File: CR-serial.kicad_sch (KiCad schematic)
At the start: 34 parts, among them J1 USB_B, J2 GPIO, J3 UART0, J4 UART1, J5 UART2, J6 UART3_HV, J7 RS232_0, J8 RS232_1, U1 CP2108-xxx-xM, U2 MAX232

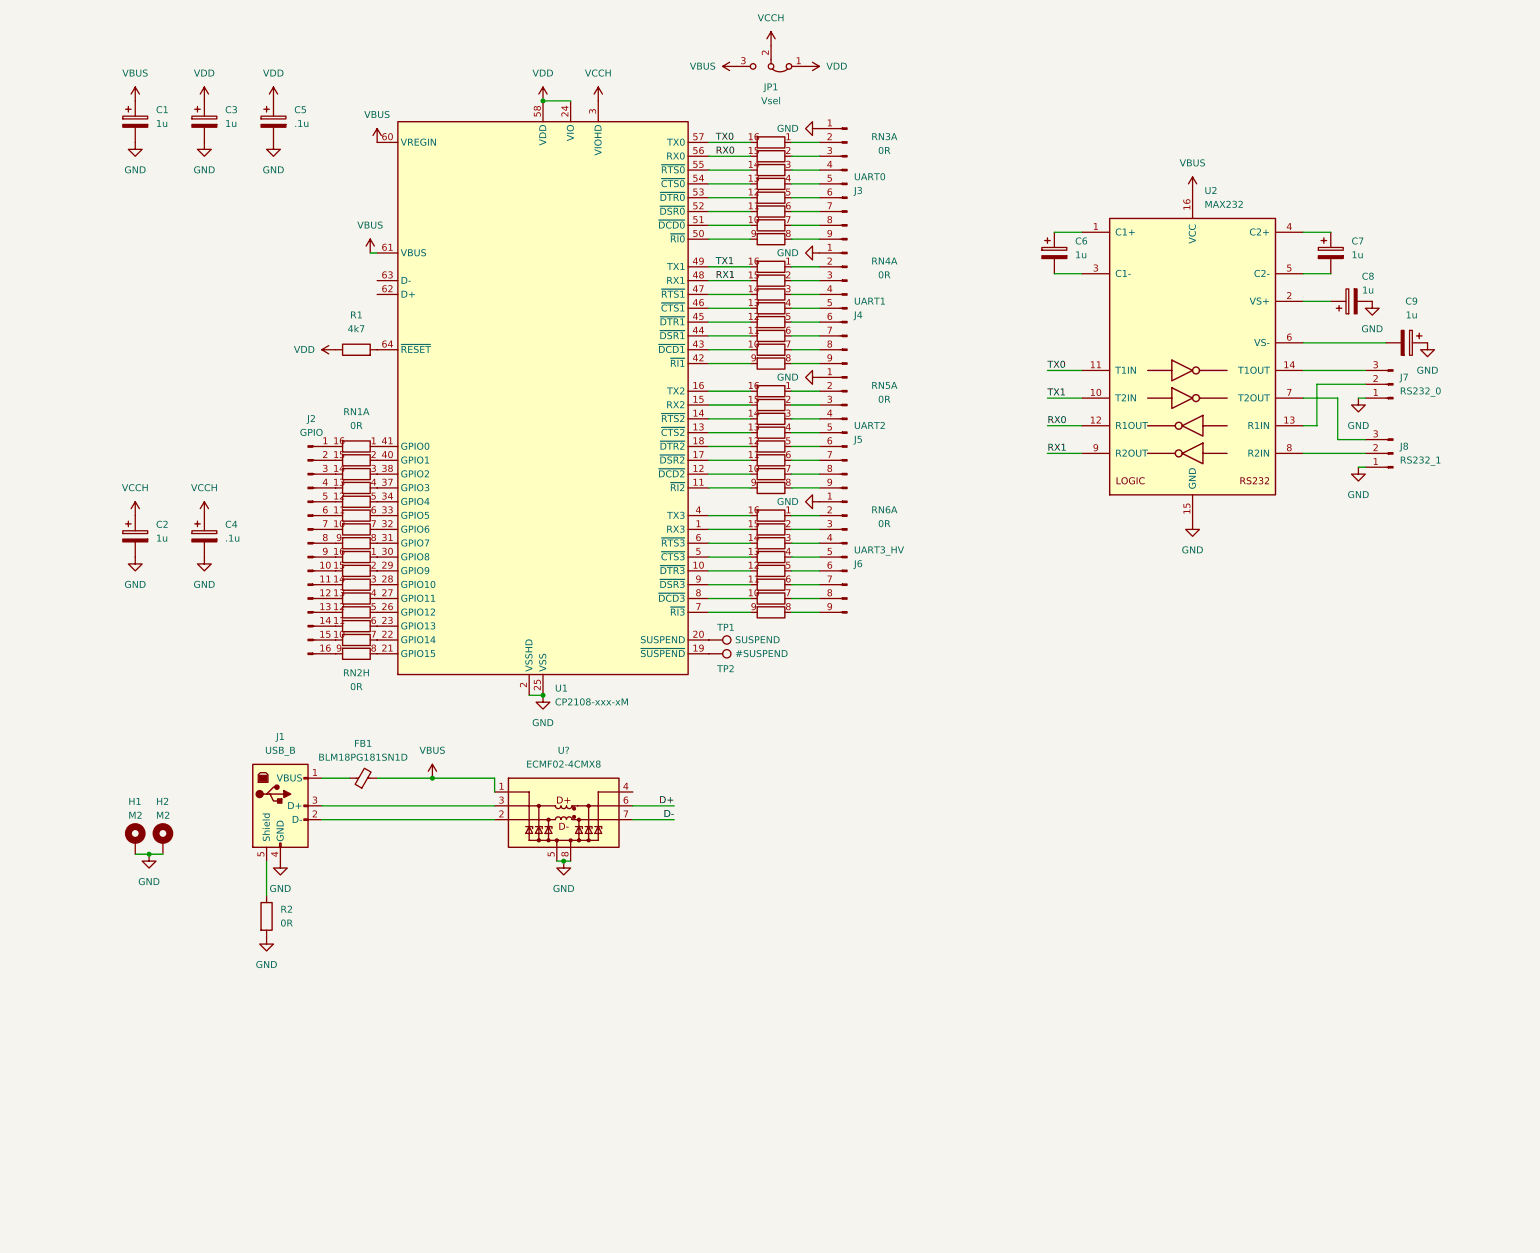
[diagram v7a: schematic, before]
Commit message: UARTs: Rework ESD protection, use individual Rs, add TVS
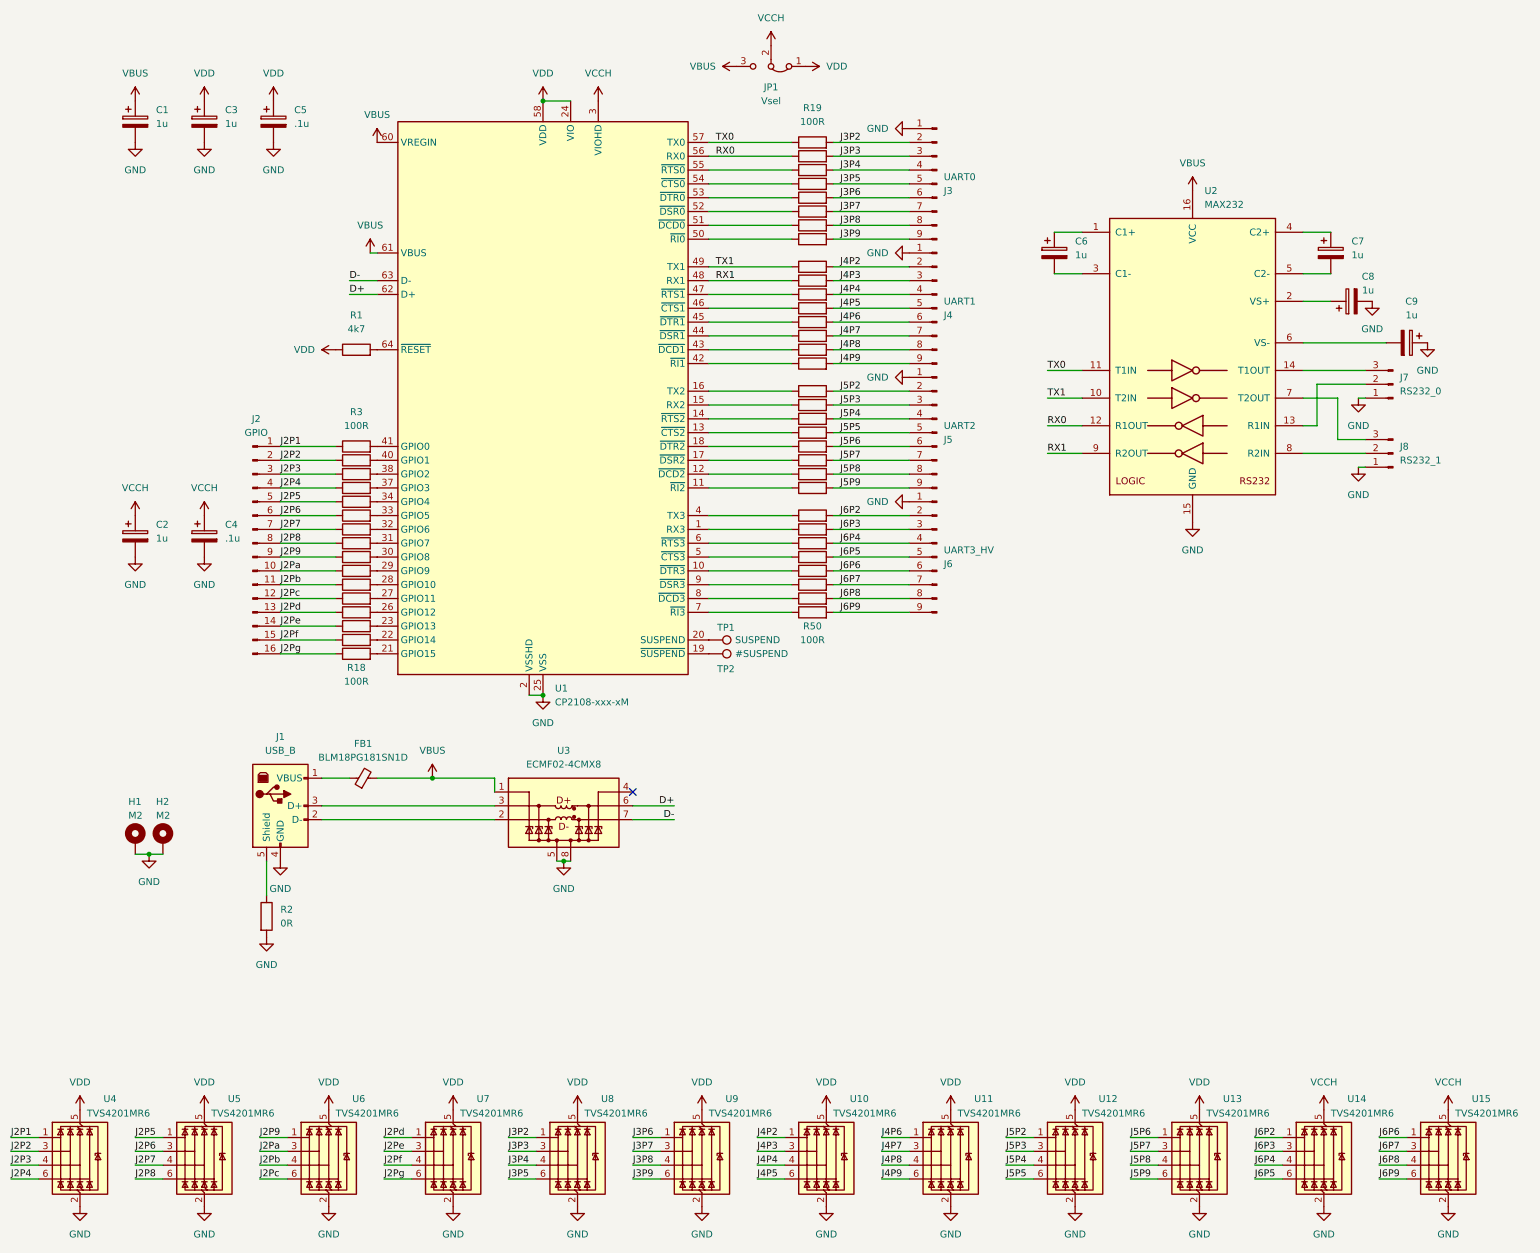
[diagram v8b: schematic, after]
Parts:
- removed RN1, RN2, RN3, RN4, RN5, RN6: 0R, Resistor_SMD:R_Array_Convex_8x0602, symbol Device:R_Pack08_Split
- added R10, R11, R12, R13, R14, R15, R16, R17, R18, R19, R20, R21, R22, R23, R24, R25, R26, R27, R28, R29, R3, R30, R31, R32, R33, R34, R35, R36, R37, R38, R39, R4, R40, R41, R42, R43, R44, R45, R46, R47, R48, R49, R5, R50, R6, R7, R8, R9: 100R, Resistor_SMD:R_0603_1608Metric, symbol Device:R
- added U10, U11, U12, U13, U14, U15, U4, U5, U6, U7, U8, U9: TVS4201MR6, Package_SO:TSOP-6_1.65x3.05mm_P0.95mm, symbol QCP_parts:TVS4201MR6
- gave numbers to parts that had none: 1
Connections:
- net D+: now also U1.62 (D+)
- net D-: now also U1.63 (D-)
- net GND: now also U10.2 (GND), U11.2 (GND), U12.2 (GND), U13.2 (GND), U14.2 (GND), U15.2 (GND), U4.2 (GND), U5.2 (GND), U6.2 (GND), U7.2 (GND), U8.2 (GND), U9.2 (GND)
- net RX0: now also R20.1
- net RX1: now also R28.1
- net TX0: now also R19.1
- net TX1: now also R27.1
- net VCCH: now also U14.5 (VBUS), U15.5 (VBUS)
- net VDD: now also U10.5 (VBUS), U11.5 (VBUS), U12.5 (VBUS), U13.5 (VBUS), U4.5 (VBUS), U5.5 (VBUS), U6.5 (VBUS), U7.5 (VBUS), U8.5 (VBUS), U9.5 (VBUS)
- net at U1.1 (RX3): now also R44.1
- net at U1.10 (~{DTR3}): now also R47.1
- net at U1.11 (~{RI2}): now also R42.1
- net at U1.12 (~{DCD2}): now also R41.1
- net at U1.13 (~{CTS2}): now also R38.1
- net at U1.14 (~{RTS2}): now also R37.1
- net at U1.15 (RX2): now also R36.1
- net at U1.16 (TX2): now also R35.1
- net at U1.17 (~{DSR2}): now also R40.1
- net at U1.18 (~{DTR2}): now also R39.1
- net at U1.21 (GPIO15): now also R18.2
- net at U1.22 (GPIO14): now also R17.2
- net at U1.23 (GPIO13): now also R16.2
- net at U1.26 (GPIO12): now also R15.2
- net at U1.27 (GPIO11): now also R14.2
- net at U1.28 (GPIO10): now also R13.2
- net at U1.29 (GPIO9): now also R12.2
- net at U1.30 (GPIO8): now also R11.2
- net at U1.31 (GPIO7): now also R10.2
- net at U1.32 (GPIO6): now also R9.2
- net at U1.33 (GPIO5): now also R8.2
- net at U1.34 (GPIO4): now also R7.2
- net at U1.37 (GPIO3): now also R6.2
- net at U1.38 (GPIO2): now also R5.2
- net at U1.4 (TX3): now also R43.1
- net at U1.40 (GPIO1): now also R4.2
- net at U1.41 (GPIO0): now also R3.2
- net at U1.42 (~{RI1}): now also R34.1
- net at U1.43 (~{DCD1}): now also R33.1
- net at U1.44 (~{DSR1}): now also R32.1
- net at U1.45 (~{DTR1}): now also R31.1
- net at U1.46 (~{CTS1}): now also R30.1
- net at U1.47 (~{RTS1}): now also R29.1
- net at U1.5 (~{CTS3}): now also R46.1
- net at U1.50 (~{RI0}): now also R26.1
- net at U1.51 (~{DCD0}): now also R25.1
- net at U1.52 (~{DSR0}): now also R24.1
- net at U1.53 (~{DTR0}): now also R23.1
- net at U1.54 (~{CTS0}): now also R22.1
- net at U1.55 (~{RTS0}): now also R21.1
- net at U1.6 (~{RTS3}): now also R45.1
- net at U1.7 (~{RI3}): now also R50.1
- net at U1.8 (~{DCD3}): now also R49.1
- net at U1.9 (~{DSR3}): now also R48.1
- net J4P5: now reaches J4.5 (Pin_5)
- net J4P5: now also R30.2, U10.6 (I/O4)
- net J5P2: now reaches J5.2 (Pin_2)
- net J5P2: now also R35.2, U12.1 (I/O1)
- net J3P8: now reaches J3.8 (Pin_8)
- net J3P8: now also R25.2, U9.4 (I/O3)
- net J2P1: now reaches J2.1 (Pin_1)
- net J2P1: now also R3.1, U4.1 (I/O1)
- net J2Pd: now reaches J2.13 (Pin_13)
- net J2Pd: now also R15.1, U7.1 (I/O1)
- net J6P9: now reaches J6.9 (Pin_9)
- net J6P9: now also R50.2, U15.6 (I/O4)
- net J4P6: now reaches J4.6 (Pin_6)
- net J4P6: now also R31.2, U11.1 (I/O1)
- net J5P3: now reaches J5.3 (Pin_3)
- net J5P3: now also R36.2, U12.3 (I/O2)
- net J5P4: now reaches J5.4 (Pin_4)
- net J5P4: now also R37.2, U12.4 (I/O3)
- net J5P5: now reaches J5.5 (Pin_5)
- net J5P5: now also R38.2, U12.6 (I/O4)
- net J5P6: now reaches J5.6 (Pin_6)
- net J5P6: now also R39.2, U13.1 (I/O1)
- net J5P7: now reaches J5.7 (Pin_7)
- net J5P7: now also R40.2, U13.3 (I/O2)
- net J5P8: now reaches J5.8 (Pin_8)
- net J5P8: now also R41.2, U13.4 (I/O3)
- net J5P9: now reaches J5.9 (Pin_9)
- net J5P9: now also R42.2, U13.6 (I/O4)
- net J2Pa: now reaches J2.10 (Pin_10)
- net J2Pa: now also R12.1, U6.3 (I/O2)
- net J2P4: now reaches J2.4 (Pin_4)
- net J2P4: now also R6.1, U4.6 (I/O4)
- net J6P7: now reaches J6.7 (Pin_7)
- net J6P7: now also R48.2, U15.3 (I/O2)
- net J6P2: now reaches J6.2 (Pin_2)
- net J6P2: now also R43.2, U14.1 (I/O1)
- net J6P3: now reaches J6.3 (Pin_3)
- net J6P3: now also R44.2, U14.3 (I/O2)
- net J6P4: now reaches J6.4 (Pin_4)
- net J6P4: now also R45.2, U14.4 (I/O3)
- net J6P5: now reaches J6.5 (Pin_5)
- net J6P5: now also R46.2, U14.6 (I/O4)
- net J6P6: now reaches J6.6 (Pin_6)
- net J6P6: now also R47.2, U15.1 (I/O1)
- net J6P8: now reaches J6.8 (Pin_8)
- net J6P8: now also R49.2, U15.4 (I/O3)
- net J2Pg: now reaches J2.16 (Pin_16)
- net J2Pg: now also R18.1, U7.6 (I/O4)
- net J3P3: now reaches J3.3 (Pin_3)
- net J3P3: now also R20.2, U8.3 (I/O2)
- net J2Pc: now reaches J2.12 (Pin_12)
- net J2Pc: now also R14.1, U6.6 (I/O4)
- net J3P7: now reaches J3.7 (Pin_7)
- net J3P7: now also R24.2, U9.3 (I/O2)
- net J3P2: now reaches J3.2 (Pin_2)
- net J3P2: now also R19.2, U8.1 (I/O1)
- net J3P4: now reaches J3.4 (Pin_4)
- net J3P4: now also R21.2, U8.4 (I/O3)
- net J3P5: now reaches J3.5 (Pin_5)
- net J3P5: now also R22.2, U8.6 (I/O4)
- net J3P6: now reaches J3.6 (Pin_6)
- net J3P6: now also R23.2, U9.1 (I/O1)
- net J3P9: now reaches J3.9 (Pin_9)
- net J3P9: now also R26.2, U9.6 (I/O4)
- net J4P8: now reaches J4.8 (Pin_8)
- net J4P8: now also R33.2, U11.4 (I/O3)
- net J4P2: now reaches J4.2 (Pin_2)
- net J4P2: now also R27.2, U10.1 (I/O1)
- net J4P3: now reaches J4.3 (Pin_3)
- net J4P3: now also R28.2, U10.3 (I/O2)
- net J4P4: now reaches J4.4 (Pin_4)
- net J4P4: now also R29.2, U10.4 (I/O3)
- net J4P7: now reaches J4.7 (Pin_7)
- net J4P7: now also R32.2, U11.3 (I/O2)
- net J4P9: now reaches J4.9 (Pin_9)
- net J4P9: now also R34.2, U11.6 (I/O4)
- net J2Pe: now reaches J2.14 (Pin_14)
- net J2Pe: now also R16.1, U7.3 (I/O2)
- net J2P9: now reaches J2.9 (Pin_9)
- net J2P9: now also R11.1, U6.1 (I/O1)
- net J2P3: now reaches J2.3 (Pin_3)
- net J2P3: now also R5.1, U4.4 (I/O3)
- net J2P6: now reaches J2.6 (Pin_6)
- net J2P6: now also R8.1, U5.3 (I/O2)
- net J2Pf: now reaches J2.15 (Pin_15)
- net J2Pf: now also R17.1, U7.4 (I/O3)
- net J2P5: now reaches J2.5 (Pin_5)
- net J2P5: now also R7.1, U5.1 (I/O1)
- net J2P8: now reaches J2.8 (Pin_8)
- net J2P8: now also R10.1, U5.6 (I/O4)
- net J2P7: now reaches J2.7 (Pin_7)
- net J2P7: now also R9.1, U5.4 (I/O3)
- net J2Pb: now reaches J2.11 (Pin_11)
- net J2Pb: now also R13.1, U6.4 (I/O3)
- net J2P2: now reaches J2.2 (Pin_2)
- net J2P2: now also R4.1, U4.3 (I/O2)
- no-connect marks 0 -> 1
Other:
- moved on the sheet: J2, J3, J4, J5, J6
